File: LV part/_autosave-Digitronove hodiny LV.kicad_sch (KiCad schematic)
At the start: 92 parts, among them J1 DD4012SB_3V3, J10 Output, J11 Output, J12 Output, J13 -, J14 9V to 170V, J15 Output, J16 Output, J17 Output, J18 Output, J19 Output, J2 +, J20 Output, J21 Output, J22 Output, J24 RCWL-0516, J25 Output, J26 Output, J27 Output, J28 Output, J29 Output, J3 Output, J30 Output, J31 Output, J32 Output, J33 Output, J34 Output, J35 Output, J36 Output, J37 Output, J38 Output, J39 Output, J4 Output, J40 Output, J41 Output, J42 Output, J43 Output, J5 Output, J6 Output, J7 Output, J8 Output, J9 Output, SW1 RESET, SW2 START/STOP, SW3 +1, SW4 SWITCH, U1 74HC595, U2 74HC595, U3 ESP32-WROOM-32, U4 74HC595, U5 74HC595, U6 74HC595, U7 74HC595

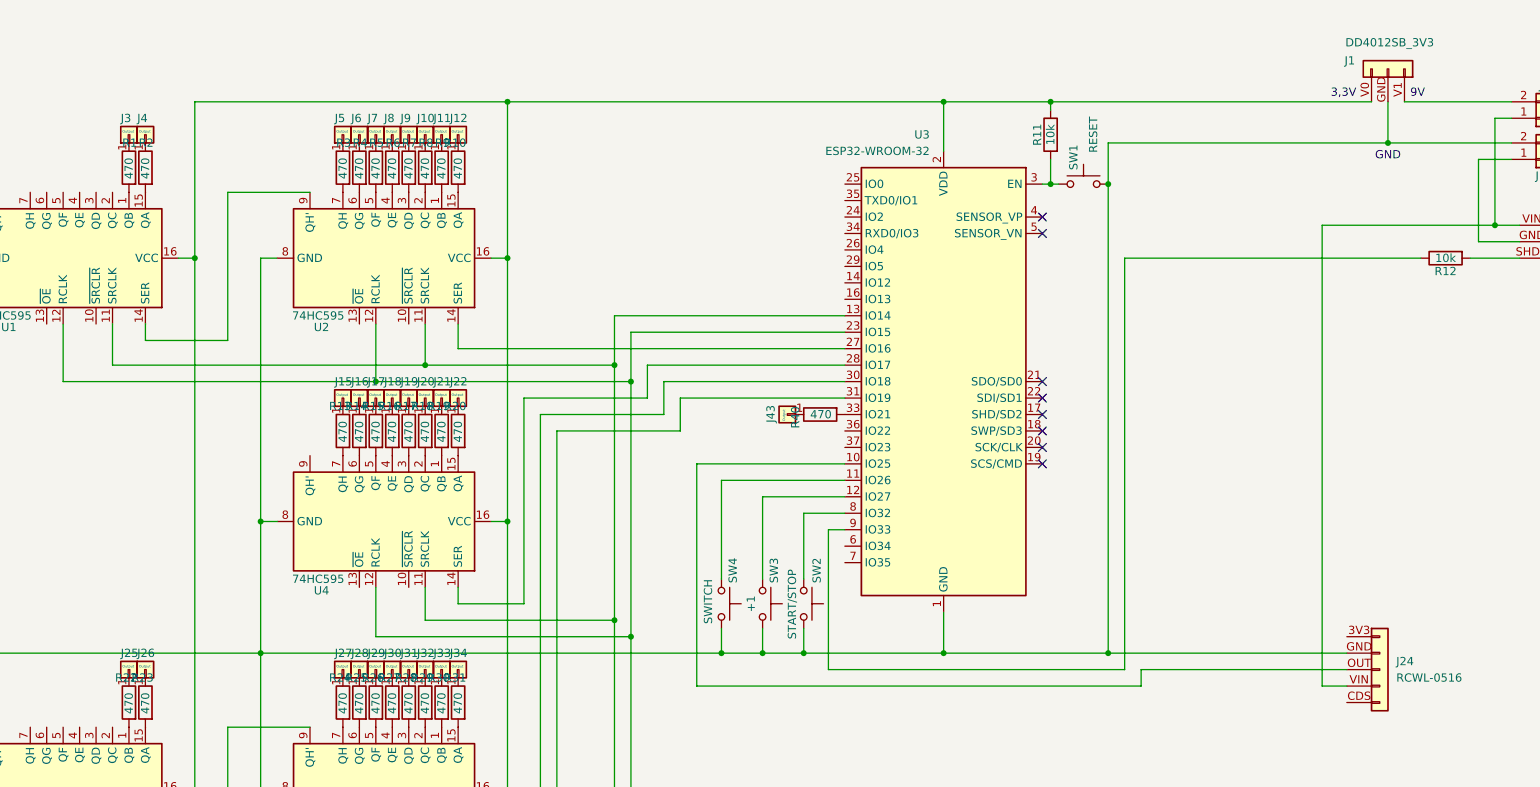
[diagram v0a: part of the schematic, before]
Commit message: Dodání pouzder
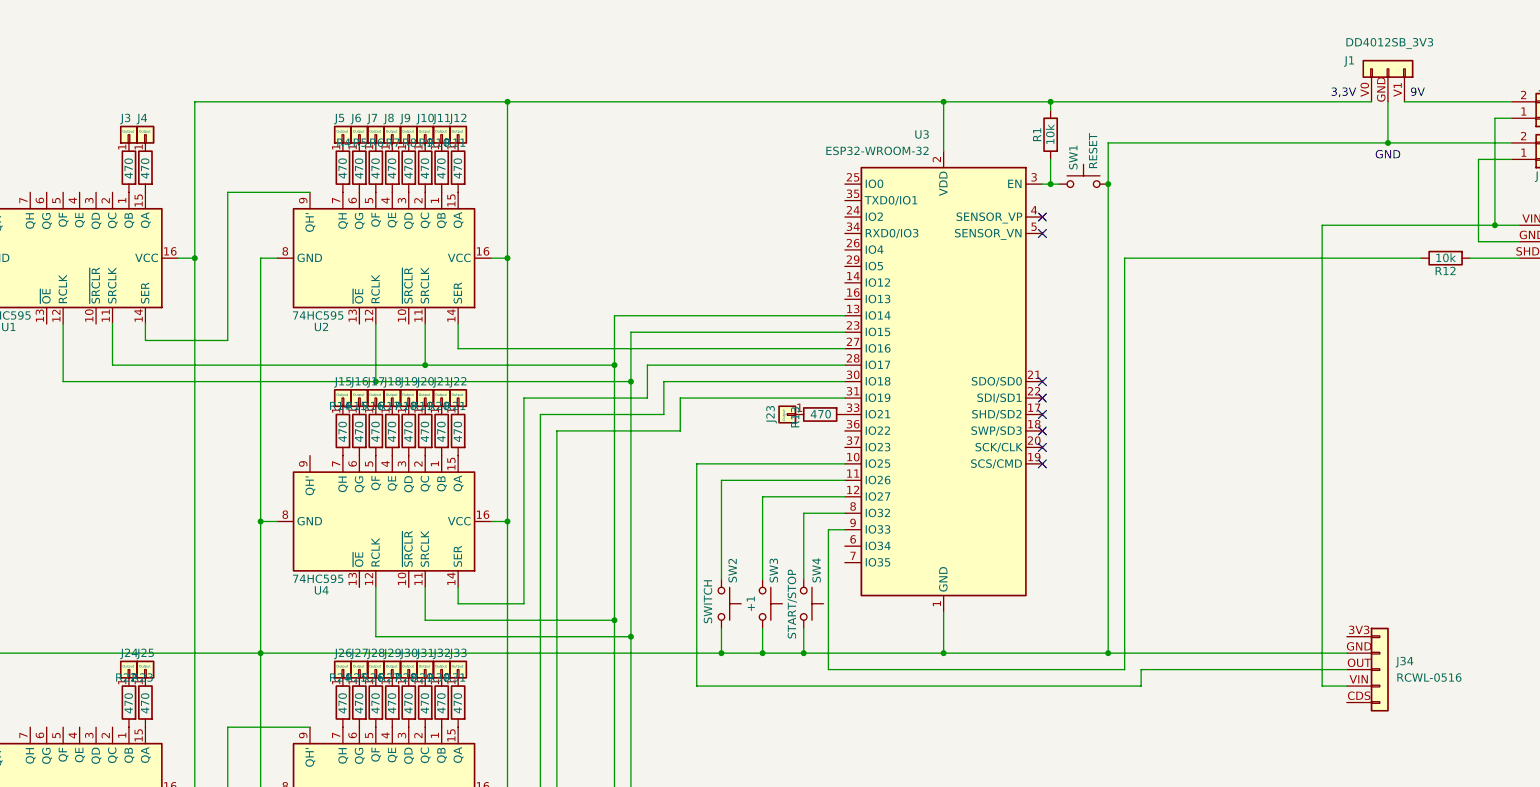
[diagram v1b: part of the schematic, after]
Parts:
- removed J34: Output, symbol Connector_Generic:Conn_01x01
- removed R1, R3, R40: 470, symbol Device:R
- added J24: Output, Connector_PinHeader_2.00mm:PinHeader_1x01_P2.00mm_Horizontal, symbol Connector_Generic:Conn_01x01
- added R11, R2, R21: 470, Resistor_SMD:R_1206_3216Metric_Pad1.30x1.75mm_HandSolder, symbol Device:R
- J10, J11, J12, J15, J16, J17, J18, J19, J20, J21, J22, J25, J26, J27, J28, J29, J3, J30, J31, J32, J33, J35, J36, J37, J38, J39, J4, J40, J41, J42, J5, J6, J7, J8, J9: footprint (none) -> Connector_PinHeader_2.00mm:PinHeader_1x01_P2.00mm_Horizontal
- J23: renamed from J43; footprint (none) -> Connector_PinHeader_2.00mm:PinHeader_1x01_P2.00mm_Horizontal
- R1: renamed from R11; footprint (none) -> Resistor_SMD:R_1206_3216Metric_Pad1.30x1.75mm_HandSolder
- R10, R12, R13, R14, R15, R16, R17, R18, R19, R20, R22, R23, R24, R25, R26, R27, R28, R29, R30, R31, R32, R33, R34, R35, R36, R37, R38, R39, R4, R5, R6, R7, R8, R9: footprint (none) -> Resistor_SMD:R_1206_3216Metric_Pad1.30x1.75mm_HandSolder
- R3: renamed from R2; footprint (none) -> Resistor_SMD:R_1206_3216Metric_Pad1.30x1.75mm_HandSolder
- renumbered J24 to J34, SW4 to SW2, SW2 to SW4
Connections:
- net at J26.1 (Pin_1): now also R24.1; no longer R23.1
- net at R7.1: now also J8.1 (Pin_1); no longer J9.1 (Pin_1)
- net at R7.2: now also U2.4 (QE); no longer U2.3 (QD)
- net at R6.1: now also J7.1 (Pin_1); no longer J8.1 (Pin_1)
- net at J11.1 (Pin_1): now also R10.1; no longer R9.1
- net at R22.1: now also J24.1 (Pin_1); no longer J25.1 (Pin_1)
- net at R14.1: now also J15.1 (Pin_1); no longer J16.1 (Pin_1)
- net at R14.2: now also U4.7 (QH); no longer U4.6 (QG)
- net at J22.1 (Pin_1): now also R21.1; no longer R20.1
- net at U4.15 (QA): now also R21.2; no longer R20.2
- net at J17.1 (Pin_1): now also R16.1; no longer R15.1
- net at U4.5 (QF): now also R16.2; no longer R15.2
- net at R18.1: now also J19.1 (Pin_1); no longer J20.1 (Pin_1)
- net at R26.1: now also J28.1 (Pin_1); no longer J29.1 (Pin_1)
- net at J12.1 (Pin_1): now also R11.1; no longer R10.1
- net at J18.1 (Pin_1): now also R17.1; no longer R16.1
- net at R29.1: now also J31.1 (Pin_1); no longer J32.1 (Pin_1)
- net at U3.33 (IO21): now also R13.2
- net at R31.1: now also J33.1 (Pin_1)
- net at U4.3 (QD): now also R18.2; no longer R17.2
- net at U4.1 (QB): now also R20.2; no longer R19.2
- net at U4.2 (QC): now also R19.2; no longer R18.2
- net at U4.4 (QE): now also R17.2; no longer R16.2
- net at R25.1: now also J27.1 (Pin_1); no longer J28.1 (Pin_1)
- net at J6.1 (Pin_1): now also R5.1; no longer R4.1
- net at R27.1: now also J29.1 (Pin_1); no longer J30.1 (Pin_1)
- net at R30.1: now also J32.1 (Pin_1); no longer J33.1 (Pin_1)
- net at R13.1: now also J23.1 (Pin_1); no longer J15.1 (Pin_1)
- net at J10.1 (Pin_1): now also R9.1; no longer R8.1
- net at U2.2 (QC): now also R9.2; no longer R8.2
- net at R19.1: now also J20.1 (Pin_1); no longer J21.1 (Pin_1)
- net at U1.1 (QB): now also R2.2
- net at J3.1 (Pin_1): now also R2.1
- net at R28.1: now also J30.1 (Pin_1); no longer J31.1 (Pin_1)
- net at R6.2: now also U2.5 (QF); no longer U2.4 (QE)
- net at U2.15 (QA): now also R11.2; no longer R10.2
- net at J5.1 (Pin_1): now also R4.1
- net at U2.7 (QH): now also R4.2
- net at U2.6 (QG): now also R5.2; no longer R4.2
- net at U2.1 (QB): now also R10.2; no longer R9.2
- new net: J25.1 (Pin_1), R23.1
- new net: R15.2, U4.6 (QG)
- new net: J9.1 (Pin_1), R8.1
- new net: R8.2, U2.3 (QD)
- new net: J21.1 (Pin_1), R20.1
- new net: J16.1 (Pin_1), R15.1
